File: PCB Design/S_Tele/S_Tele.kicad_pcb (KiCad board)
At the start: 2 copper layers, 124.2 x 46 mm, 37 parts, among them J1 Screw_Terminal_01x08, J2 Conn_01x01, J3 SMA, J4 SMA, J5 SMA, J6 SMA, J7 SMA, J8 SMA, U1 L7815, U2 L7805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

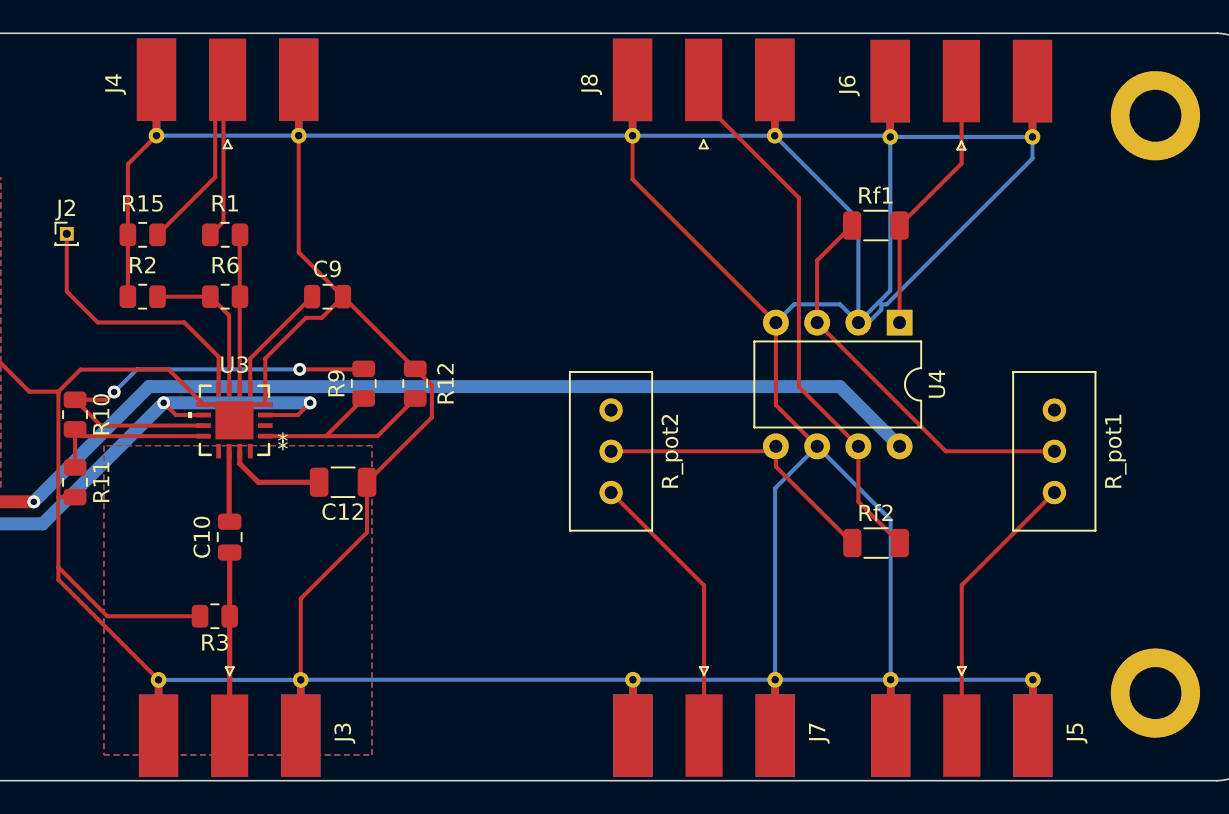
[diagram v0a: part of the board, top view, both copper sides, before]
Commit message: LM358 I/O swapped
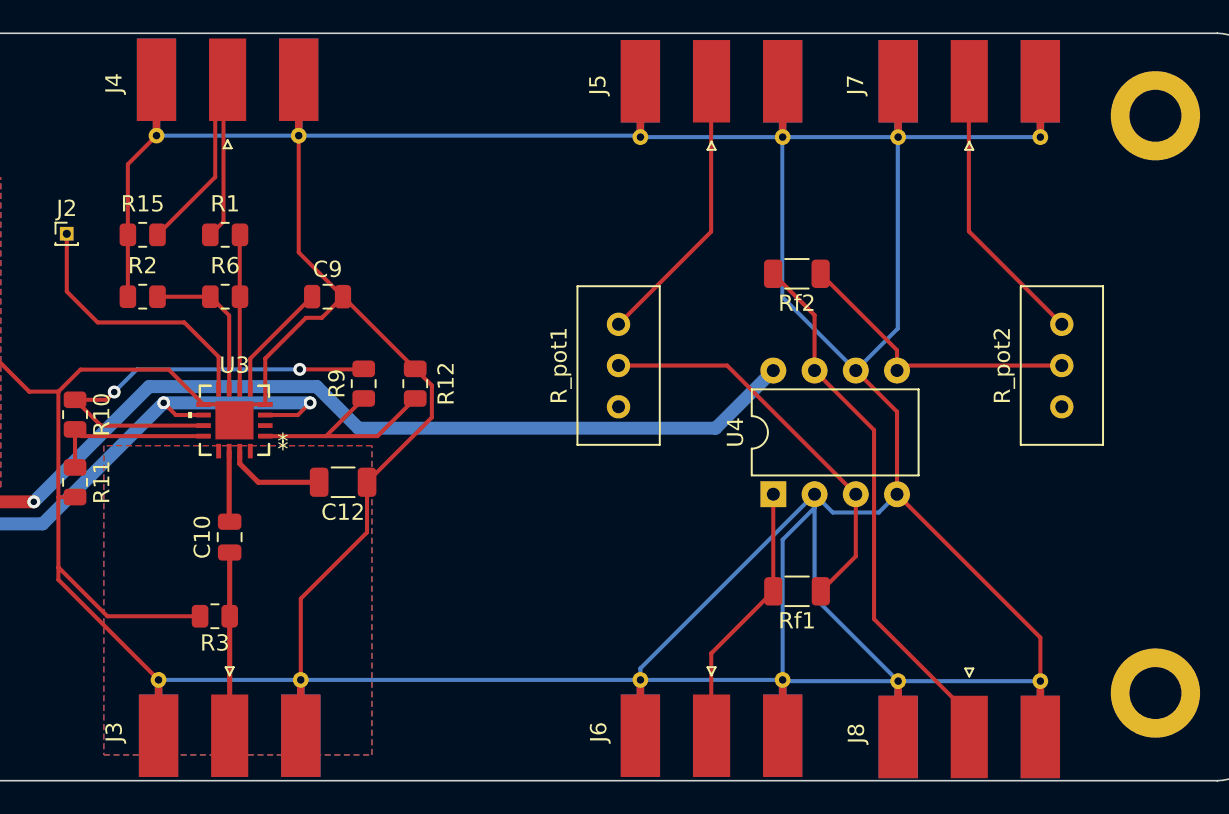
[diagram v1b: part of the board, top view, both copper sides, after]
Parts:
- moved J8 40.5 mm to (185.4, 122.9), turned to 90 degrees
- moved J7 40.3 mm to (185.4, 86.0), turned to -90 degrees
- moved J6 40.0 mm to (169.5, 122.8), turned to 90 degrees
- moved J5 40.0 mm to (169.5, 86.0), turned to -90 degrees
- moved R_pot2 29.6 mm to (191.1, 99.2), turned to 90 degrees
- moved R_pot1 28.8 mm to (163.8, 99.2), turned to 90 degrees
- moved Rf1 23.0 mm to (174.8, 115.7), turned to 180 degrees
- moved Rf2 17.3 mm to (174.8, 96.1), turned to 180 degrees
- moved U4 13.1 mm to (173.3, 109.7), turned to 90 degrees
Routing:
- net +15VDC: track 136.5 -> 129.7 mm

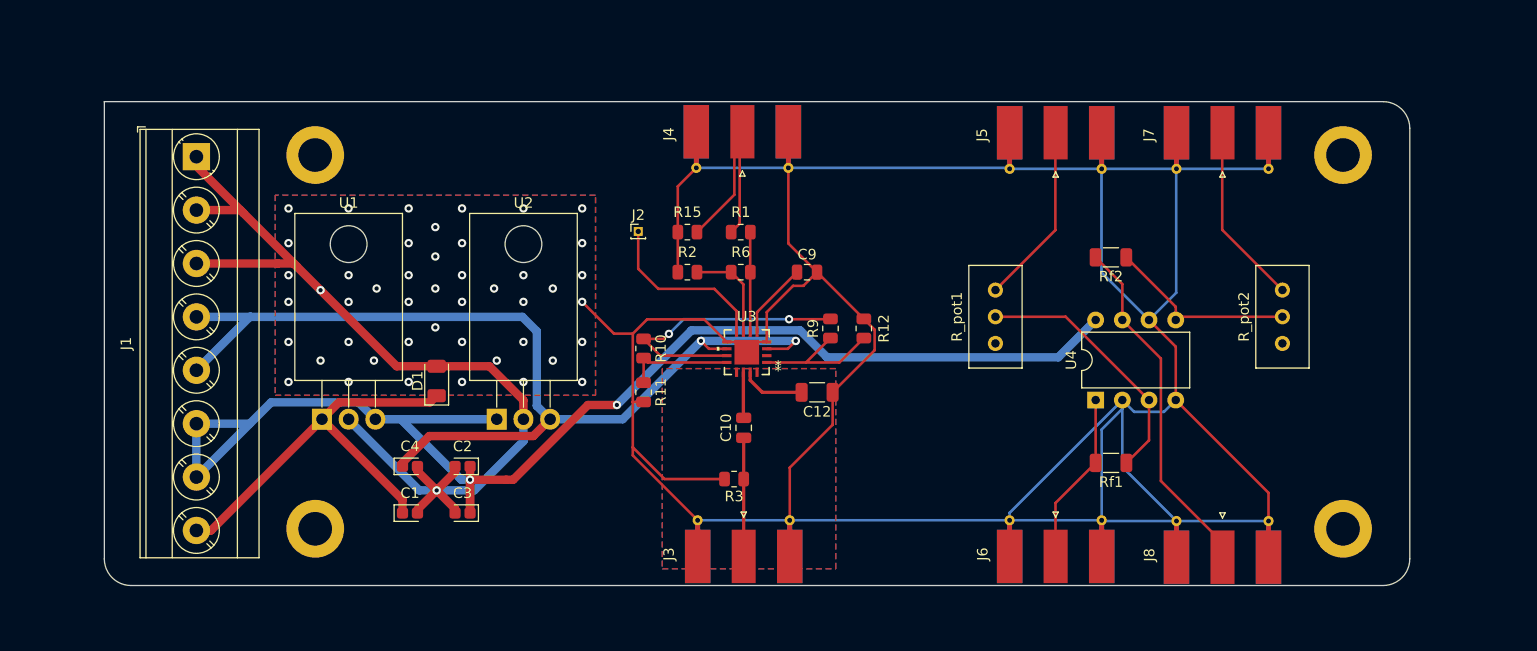
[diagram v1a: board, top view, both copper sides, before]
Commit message: RF TXline width fixed, GCPW --> CPW
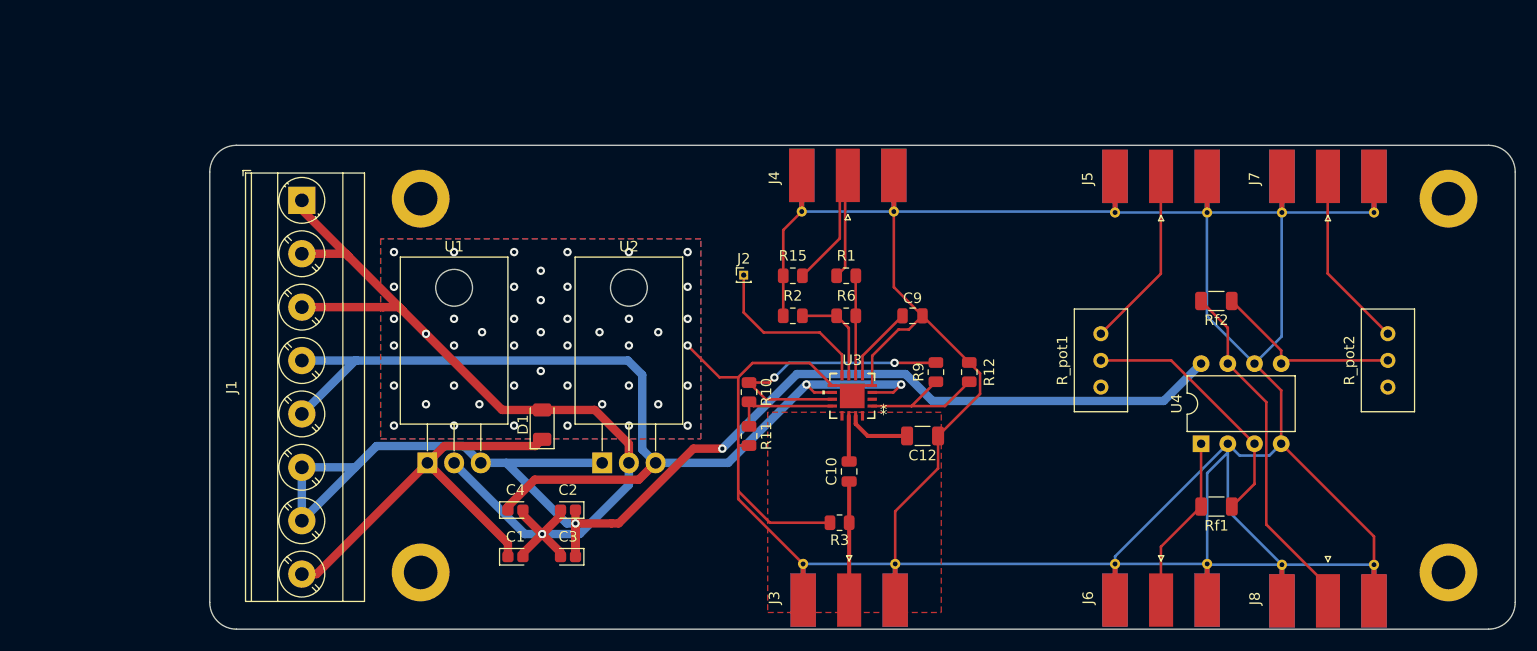
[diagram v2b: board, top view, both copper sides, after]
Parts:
- moved C10 10.9 mm to (149.9, 116.5)
- moved J3 10.9 mm to (149.9, 127.0)
- moved J4 10.9 mm to (149.7, 90.0)
- moved J6 10.9 mm to (179.5, 127.0)
- moved J8 10.9 mm to (195.4, 127.1)
- moved R1 10.9 mm to (149.6, 97.8)
- moved R10 10.9 mm to (140.3, 108.9)
- moved R11 10.9 mm to (140.3, 113.1)
- moved R6 10.9 mm to (149.6, 101.7)
- moved R9 10.9 mm to (158.1, 107.0)
- moved REF** 10.9 mm to (206.9, 90.5)
- moved REF** 10.9 mm to (206.9, 126.1)
- moved R_pot1 10.9 mm to (173.8, 103.4)
- moved U4 10.9 mm to (183.3, 113.8)
- moved C1 10.9 mm to (118.1, 124.6)
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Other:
- outline, holes or cut-outs redrawn

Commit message: Bill of materials added
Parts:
- C1, C2, C3, C4: footprint Capacitor_Tantalum_SMD:CP_EIA-1608-08_AVX-J -> Capacitor_Tantalum_SMD:CP_EIA-2012-12_Kemet-R
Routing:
- net +15VDC: track 129.7 -> 126.7 mm

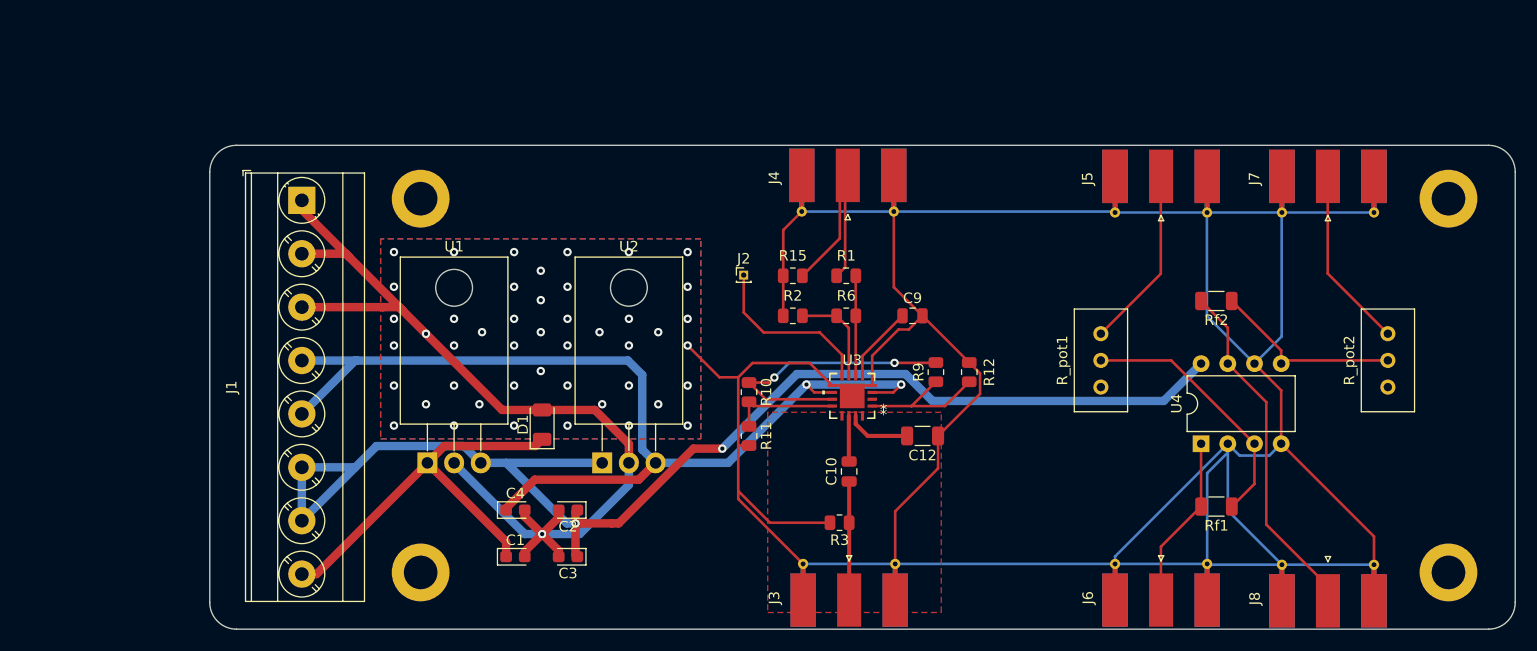
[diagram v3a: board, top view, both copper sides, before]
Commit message: CPW --> GCPW for RO4350B & silkscreen added
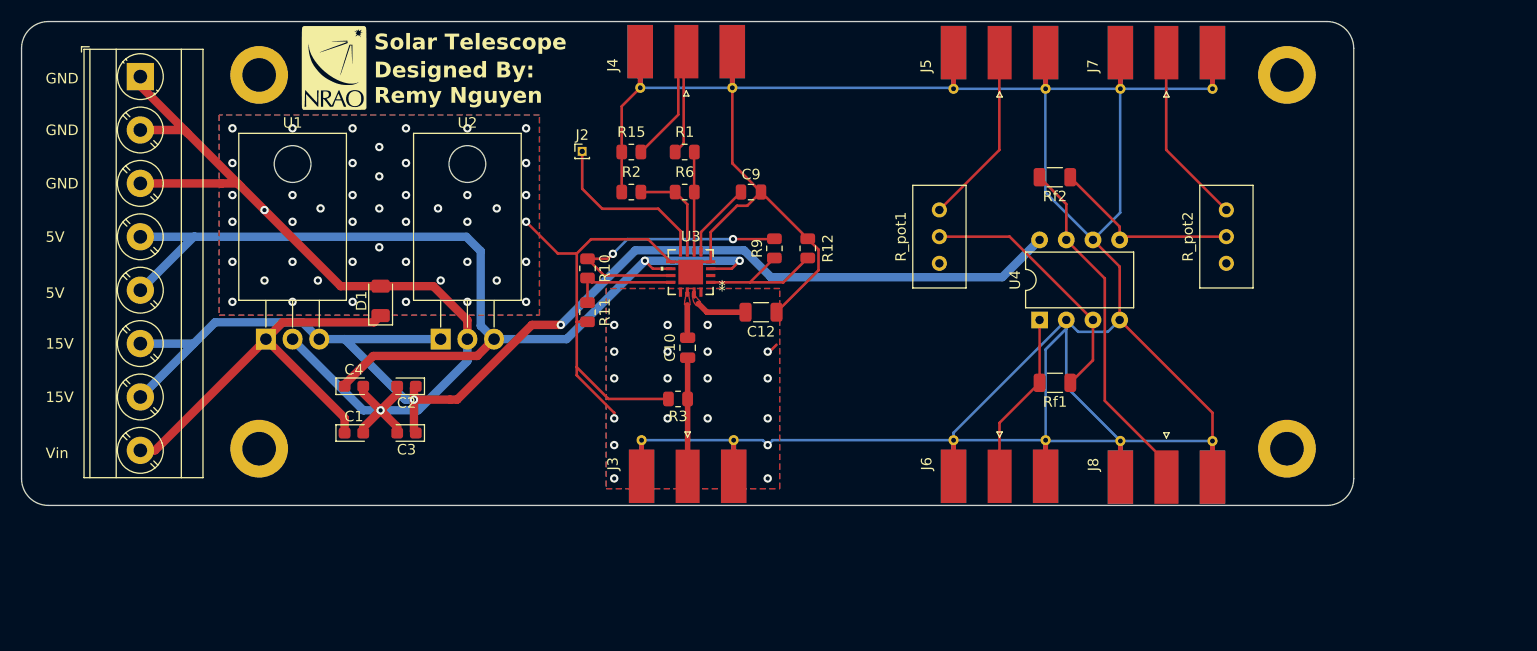
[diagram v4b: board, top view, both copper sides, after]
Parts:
- added G***: LOGO, Imports:nraoLogo8mm, F.Cu at (100.8, 78.1)
- moved C10 19.4 mm to (134.5, 104.7)
- moved J3 19.4 mm to (134.5, 115.2)
- moved J6 19.4 mm to (164.2, 115.2)
- moved R6 19.4 mm to (134.2, 89.9)
- moved R9 19.4 mm to (142.7, 95.2)
- moved REF** 19.4 mm to (191.5, 78.7)
- moved REF** 19.4 mm to (191.5, 114.3)
- moved R_pot1 19.4 mm to (158.4, 91.6)
- moved U4 19.4 mm to (168.0, 102.1)
- moved J8 19.4 mm to (180.0, 115.3)
- moved R1 19.4 mm to (134.2, 86.1)
- moved C1 19.4 mm to (102.7, 112.8)
- moved J2 19.4 mm to (124.5, 86.0)
- moved R10 19.4 mm to (125.0, 97.1)
- moved R11 19.4 mm to (125.0, 101.3)
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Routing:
- net GND: track 417.2 -> 401.8 mm, vias 47 -> 66
- net +15VDC: track 126.7 -> 121.6 mm
- net INHI: track 4.36 -> 3.13 mm
- net INLO: track 6.13 -> 5.30 mm
- added copper zone on F.Cu, net INHI
- added copper zone on F.Cu, net INLO
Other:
- board size 124.2 x 46 mm -> 126.7 x 46 mm
- board text added: "15V"
- board text added: "5V"
- board text added: "Designed By: Remy Nguyen"
- board text added: "GND"
- board text added: "Solar Telescope"
- board text added: "Vin"
